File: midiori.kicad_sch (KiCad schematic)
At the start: 86 parts, among them J1 midiori-rescue_x68000_expansi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, J2 Conn_ARM_JTAG_SWD_10, J3 AudioJack3, J4 Mini-DIN-5, J5 AudioJack3, J6 AudioJack3, J7 Conn_01x06, J8 AudioJack3, J9 Mini-DIN-5, U1 74LCX07, U10 ICE40HX1K-VQ100, U11 AP2205K-3.3, U12 AK4432, U13 TL074, U14 AP2205K-3.3, U15 TL072, U16 74LCX07, U17 PC817, U18 SN74LVC245APW, U2 AT25SF081-SSHD-X, U3 AP2127K-1.2, U4 SN74LVC245APW, U5 SN74LVC245APW, U6 SN74LVC245APW, U7 SN74LVC245APW, U8 SN74LVC245APW, U9 SN74LVC245APW, X1 16MHz, X2 24.576MHz

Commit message: aaaaaaaaaaa
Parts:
- removed C11, C13, C15, C4, C6, C9: 0.1uF, Capacitor_SMD:C_0805_2012Metric, symbol Device:C
- added JP3, JP4, JP5: Jumper_3_Bridged12, Jumper:SolderJumper-3_P1.3mm_Bridged12_Pad1.0x1.5mm, symbol Jumper:Jumper_3_Bridged12
- added unit 6 of U1
- R14: value R -> 10k; footprint (none) -> Resistor_SMD:R_0805_2012Metric
- R15, R16: footprint (none) -> Resistor_SMD:R_0805_2012Metric
- R6, R9: footprint Resistor_SMD:R_0805_2012Metric_Pad1.15x1.40mm_HandSolder -> Resistor_SMD:R_0805_2012Metric
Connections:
- net +3V3: now also U18.1 (DIR), U8.1 (DIR)
- net 10m: now also U10.89 (IOT_84_GBIN1); no longer U10.97 (IOT_91)
- net 24.576mhz: now also JP5.1 (A)
- net BG: now also J1.B47 (/BG), U18.2 (A1); no longer U18.18 (B1)
- net BGACK: now also J1.B48 (/BGACK)
- net BR: now also J1.B46 (/BR)
- net DTACK: now also U18.5 (A4)
- net EXOWN: now also J1.B39 (/EXOWN), U18.4 (A3)
- net EXREQ: now also J1.B36 (/EXREQ)
- net GND: now also U18.11 (B8), U18.12 (B7), U18.13 (B6), U18.7 (A6), U18.8 (A7), U18.9 (A8); no longer U18.1 (DIR), U8.1 (DIR)
- net IDDIR: now also U8.9 (A8), JP3.1 (A)
- net RW: now also U16.8
- net UDS: now also U18.3 (A2), U1.12; no longer U16.8, U18.17 (B2)
- net addr_dir: now also JP4.3 (B); no longer U10.69 (IOR_68)
- net bg: now also U18.18 (B1); no longer U18.2 (A1)
- net bick: now also JP5.2 (C); no longer U10.89 (IOT_84_GBIN1)
- net data_dir: now also U10.69 (IOR_68), JP3.2 (C), JP3.3 (B); no longer U10.96 (IOT_90)
- net dtack: now also U10.82 (IOT_78), U18.15 (B4); no longer U1.5, U10.93 (IOT_87)
- net exown: now also U10.97 (IOT_91), U18.16 (B3); no longer U10.82 (IOT_78), U16.1
- net rw_drv: now also U16.9
- net uds: now also U18.17 (B2), JP4.1 (A); no longer U10.83 (IOT_79), U18.3 (A2)
- net uds_lds_drv: now also U1.13; no longer U16.9
- net EXACK: now reaches J1.B37 (/EXACK)
- net EXACK: now also U18.6 (A5)
- net iddir: now reaches U8.11 (B8)
- net iddir: now also U10.96 (IOT_90)
- net exack: now reaches U18.14 (B5)
- net exreq renamed exreq_drv
- new net: JP4.2 (C), JP5.3 (B), U10.83 (IOT_79)
- new net dtack_drv: U1.5, U10.93 (IOT_87)
- new net exown_drv: U16.1
- no-connect marks 48 -> 33
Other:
- moved on the sheet: U16D

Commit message: swap optos
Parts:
- removed JP3, JP4, JP5: Jumper_3_Bridged12, Jumper:SolderJumper-3_P1.3mm_Bridged12_Pad1.0x1.5mm, symbol Jumper:Jumper_3_Bridged12
- removed U10: ICE40HX1K-VQ100, ICE40HX1K-VQ100:QFP50P1600X1600X120-100N, symbol midiori-rescue:ICE40HX1K-VQ100-ICE40HX1K-VQ100-midiori-rescue-midiori-rescue
- added C11, C13, C4, C6, C9: 0.1uF, Capacitor_SMD:C_0805_2012Metric, symbol Device:C
- added U10: ICE40HX1K-TQ144, Package_QFP:TQFP-144_20x20mm_P0.5mm, symbol FPGA_Lattice:ICE40HX1K-TQ144
- J1: footprint x68k:x68000_expansion -> x68k:x68000_expansion_vias
- U17: value PC817 -> H11L1; footprint Package_DIP:DIP-4_W7.62mm -> Package_DIP:SMDIP-6_W9.53mm; symbol Isolator:PC817 -> Isolator:H11L1
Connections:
- net +1V2: now also U10.111 (VCC), U10.27 (VCC), U10.36 (VCCPLL), U10.51 (VCC), U10.92 (VCC)
- net +3V3: now also U17.6, C11.1, C13.1, C4.1, C6.1, C9.1, U10.100 (VCCIO_1), U10.108 (VPP_2V5), U10.123 (VCCIO_0), U10.133 (VCCIO_0), U10.30 (VCCIO_3), U10.46 (VCCIO_2), U10.57 (VCCIO_2), U10.6 (VCCIO_3), U10.72 (VCC_SPI), U10.89 (VCCIO_1)
- net 10MHz: now also U8.9 (A8); no longer U8.2 (A1)
- net 10m: now also U8.11 (B8), U10.144 (IOT_96); no longer U8.18 (B1)
- net 16mhz: now also U10.93 (IOR_60_GBIN3)
- net 24.576mhz: now also U10.94 (IOR_61_GBIN2)
- net AS: now also U16.8, U8.8 (A7); no longer U16.6, U8.6 (A5)
- net BG: now also U18.5 (A4); no longer U18.2 (A1)
- net BGACK: now also U1.2; no longer U16.10
- net BR: now also U1.4; no longer U1.10
- net DTACK: now also U16.12, U8.3 (A2); no longer U1.6, U18.5 (A4)
- net EXACK: now also U8.2 (A1); no longer U18.6 (A5)
- net EXOWN: now also U1.6, U18.8 (A7); no longer U16.2, U18.4 (A3)
- net EXREQ: now also U16.2; no longer U16.4
- net EXRESET: now also U18.9 (A8); no longer U8.3 (A2)
- net GND: now also U17.5, C11.2, C13.2, C4.2, C6.2, C9.2, U10.103 (GND), U10.13 (GND), U10.132 (GND), U10.14 (GND), U10.140 (GND), U10.35 (GNDPLL), U10.5 (GND), U10.59 (GND), U10.69 (GND), U10.86 (GND); no longer U17.3, U18.11 (B8), U18.12 (B7), U18.13 (B6), U18.7 (A6), U18.8 (A7), U18.9 (A8)
- net IACK2: now also U18.7 (A6); no longer U8.7 (A6)
- net IACK4: now also U18.6 (A5); no longer U8.8 (A7)
- net IDDIR: now also U8.4 (A3); no longer U8.9 (A8)
- net IRQ2: now also U1.8; no longer U1.2
- net IRQ4: now also U1.10; no longer U1.4
- net LDS: now also U16.6, U8.7 (A6); no longer U16.12, U8.5 (A4)
- net RW: now also U16.4, U8.5 (A4); no longer U16.8, U8.4 (A3)
- net UDS: now also J1.A29 (/UDS), U16.10, U8.6 (A5); no longer U1.12, U18.3 (A2)
- net a1: now also U10.58 (IOB_38)
- net a16: now also U10.11 (IOL_5A)
- net a17: now also U10.10 (IOL_4B)
- net a18: now also U10.9 (IOL_4A)
- net a19: now also U10.8 (IOL_3B)
- net a2: now also U10.56 (IOB_37)
- net a20: now also U10.7 (IOL_3A)
- net a21: now also U10.4 (IOL_2B)
- net a22: now also U10.3 (IOL_2A)
- net a23: now also U10.2 (IOL_1B)
- net a3: now also U10.52 (IOB_34)
- net a4: now also U10.50 (IOB_36_GBIN4)
- net a5: now also U10.49 (IOB_35_GBIN5)
- net a6: now also U10.48 (IOB_33)
- net a7: now also U10.47 (IOB_32)
- net ab10: now also U10.33 (IOL_12A)
- net ab11: now also U10.32 (IOL_11B)
- net ab12: now also U10.31 (IOL_11A)
- net ab13: now also U10.29 (IOL_10B)
- net ab14: now also U10.28 (IOL_10A)
- net ab15: now also U10.26 (IOL_9B)
- net ab9: now also U10.34 (IOL_12B)
- net addr_dir: now also U10.61 (IOB_40)
- net as: now also U8.12 (B7), U10.143 (IOT_95); no longer U8.14 (B5)
- net as_drv: now also U16.9, U10.121 (IOT_82); no longer U16.5
- net bg: now also U18.15 (B4), U10.122 (IOT_83); no longer U18.18 (B1)
- net bgack: now also U1.1, U10.107 (IOR_72); no longer U16.11
- net bick: now also U10.76 (IOR_51)
- net br: now also U1.3, U10.113 (IOT_74); no longer U1.11
- net d0: now also U10.45 (IOB_31)
- net d1: now also U10.44 (IOB_30)
- net d2: now also U10.43 (IOB_29)
- net d3: now also U10.42 (IOB_28)
- net d4: now also U10.41 (IOB_27)
- net d5: now also U10.39 (IOB_26)
- net d6: now also U10.38 (IOB_25)
- net d7: now also U10.37 (IOB_24)
- net data_dir: now also U10.60 (IOB_39)
- net db10: now also U10.23 (IOL_8A)
- net db11: now also U10.22 (IOL_7B)
- net db12: now also U10.21 (IOL_7A_GBIN6)
- net db13: now also U10.20 (IOL_6B_GBIN7)
- net db14: now also U10.19 (IOL_6A)
- net db15: now also U10.12 (IOL_5B)
- net db8: now also U10.25 (IOL_9A)
- net db9: now also U10.24 (IOL_8B)
- net dtack: now also U8.17 (B2), U10.137 (IOT_90); no longer U18.15 (B4)
- net dtack_drv: now also U16.13, U10.117 (IOT_78); no longer U1.5
- net exack: now also U8.18 (B1), U10.136 (IOT_89); no longer U18.14 (B5)
- net exown: now also U18.12 (B7), U10.134 (IOT_87); no longer U18.16 (B3)
- net exown_drv: now also U1.5, U10.114 (IOT_75); no longer U16.1
- net exreq_drv: now also U16.1, U10.116 (IOT_77); no longer U16.3
- net exreset: now also U18.11 (B8), U10.135 (IOT_88); no longer U8.17 (B2)
- net iack2: now also U18.13 (B6), U10.129 (IOT_85_GBIN0); no longer U8.13 (B6)
- net iack4: now also U18.14 (B5), U10.128 (IOT_84_GBIN1); no longer U8.12 (B7)
- net iddir: now also U8.16 (B3), U10.138 (IOT_91); no longer U8.11 (B8)
- net irq2: now also U1.9, U10.115 (IOT_76); no longer U1.1
- net irq4: now also U1.11, U10.112 (IOT_73); no longer U1.3
- net lds: now also U8.13 (B6), U10.142 (IOT_94); no longer U8.15 (B4)
- net lrck: now also U10.74 (IOR_49)
- net midi_in: now also U10.104 (IOR_69)
- net midi_out: now also U1.13, U10.105 (IOR_70); no longer U1.9
- net reset: now also U10.66 (~{CRESET_B})
- net rw: now also U8.15 (B4), U10.139 (IOT_92); no longer U8.16 (B3)
- net rw_drv: now also U16.3, U10.118 (IOT_79); no longer U16.9
- net sck: now also U10.70 (IOB_46_SCK)
- net sdti: now also U10.75 (IOR_50)
- net si: now also U10.67 (IOB_44_SDO)
- net smute: now also U10.73 (IOR_48)
- net so: now also U10.68 (IOB_45_SDI)
- net ss: now also U10.71 (IOB_47_SS)
- net uds: now also U8.14 (B5), U10.141 (IOT_93); no longer U18.17 (B2)
- net xltr_oe: now also U10.62 (IOB_41)
- net at R9.2: now also U1.12; no longer U1.8
- removed net uds_lds_drv: U1.13, U16.13
- new net lds_drv: U10.120 (IOT_81), U16.5
- new net uds_drv: U10.119 (IOT_80), U16.11
- no-connect marks 33 -> 32
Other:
- moved on the sheet: C10, C12, C14, C3, C5, C7, R3, U16A, U16B, U16C, U16D, U16E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

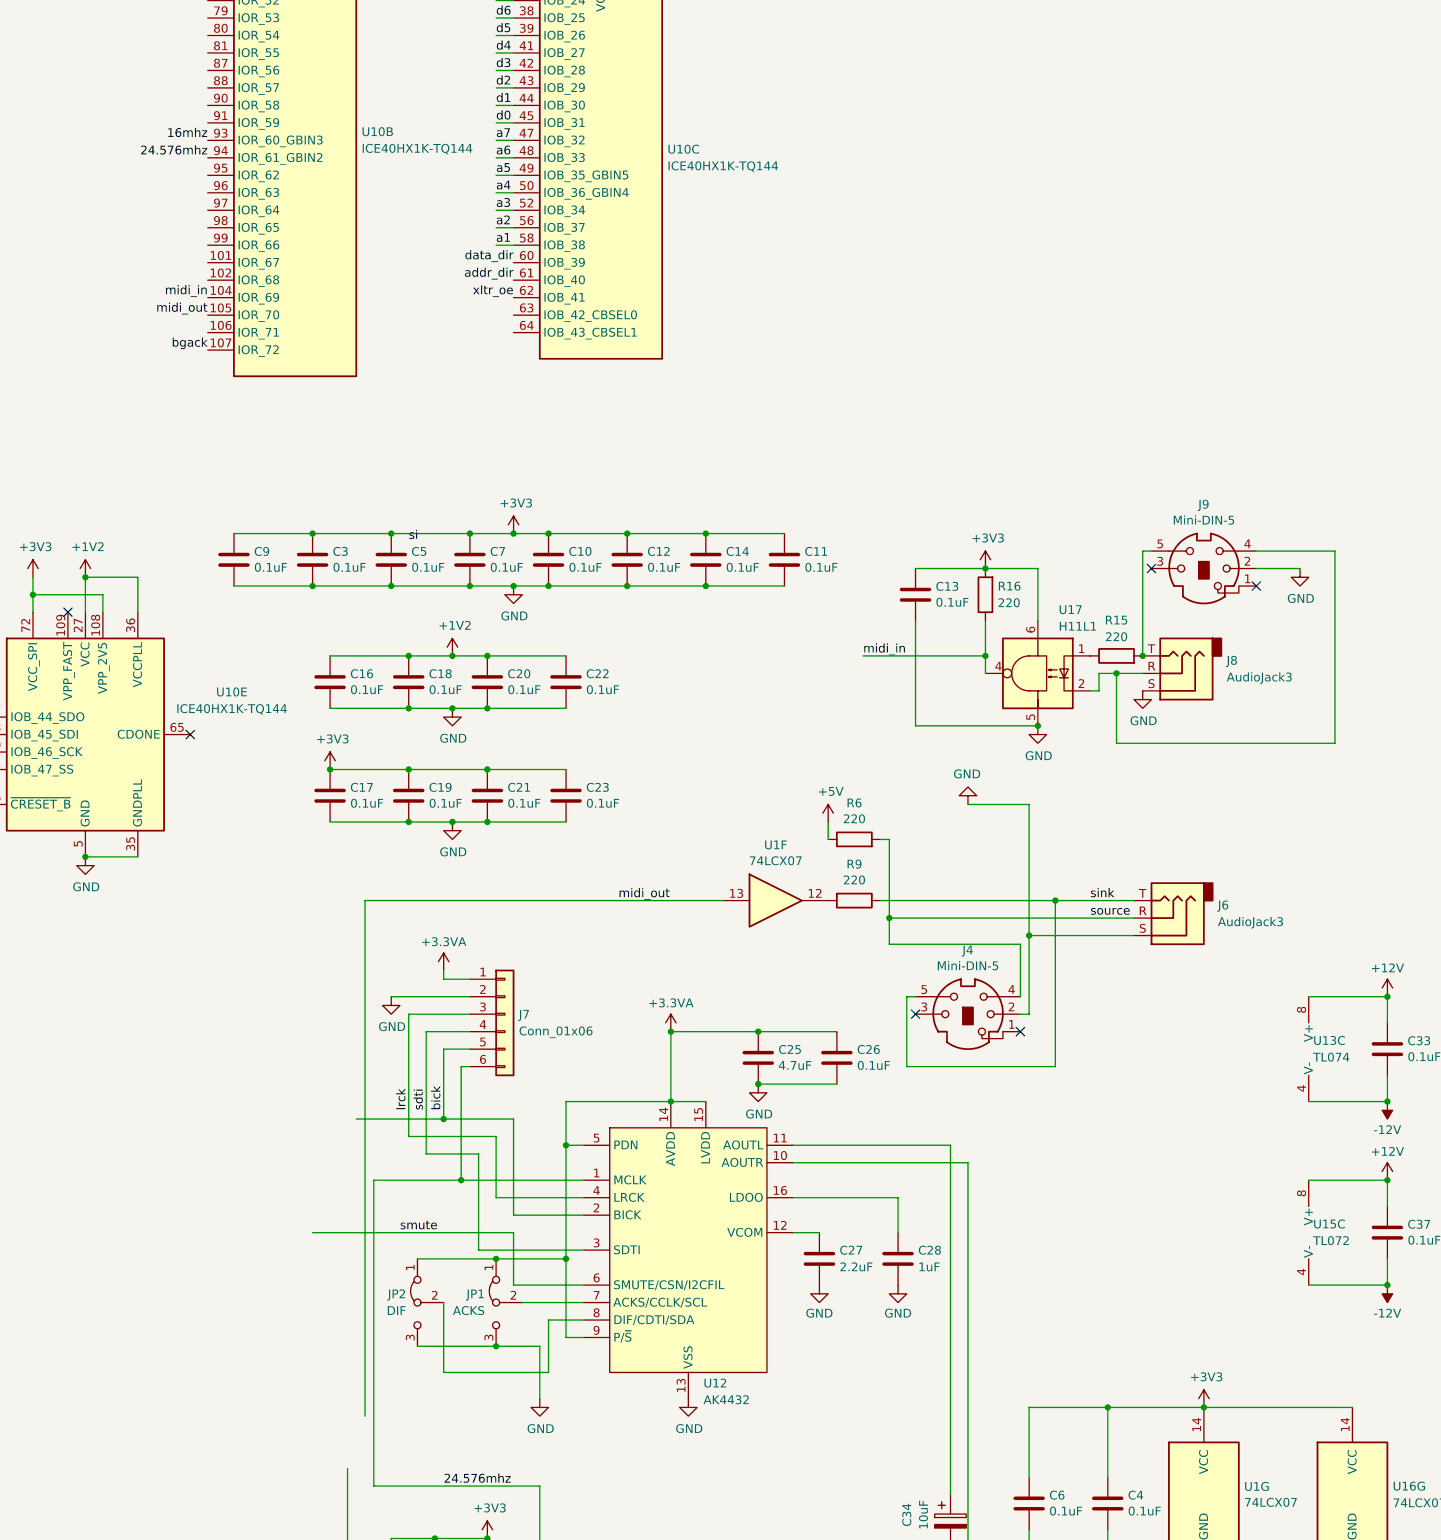
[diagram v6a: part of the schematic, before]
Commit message: crystal swap
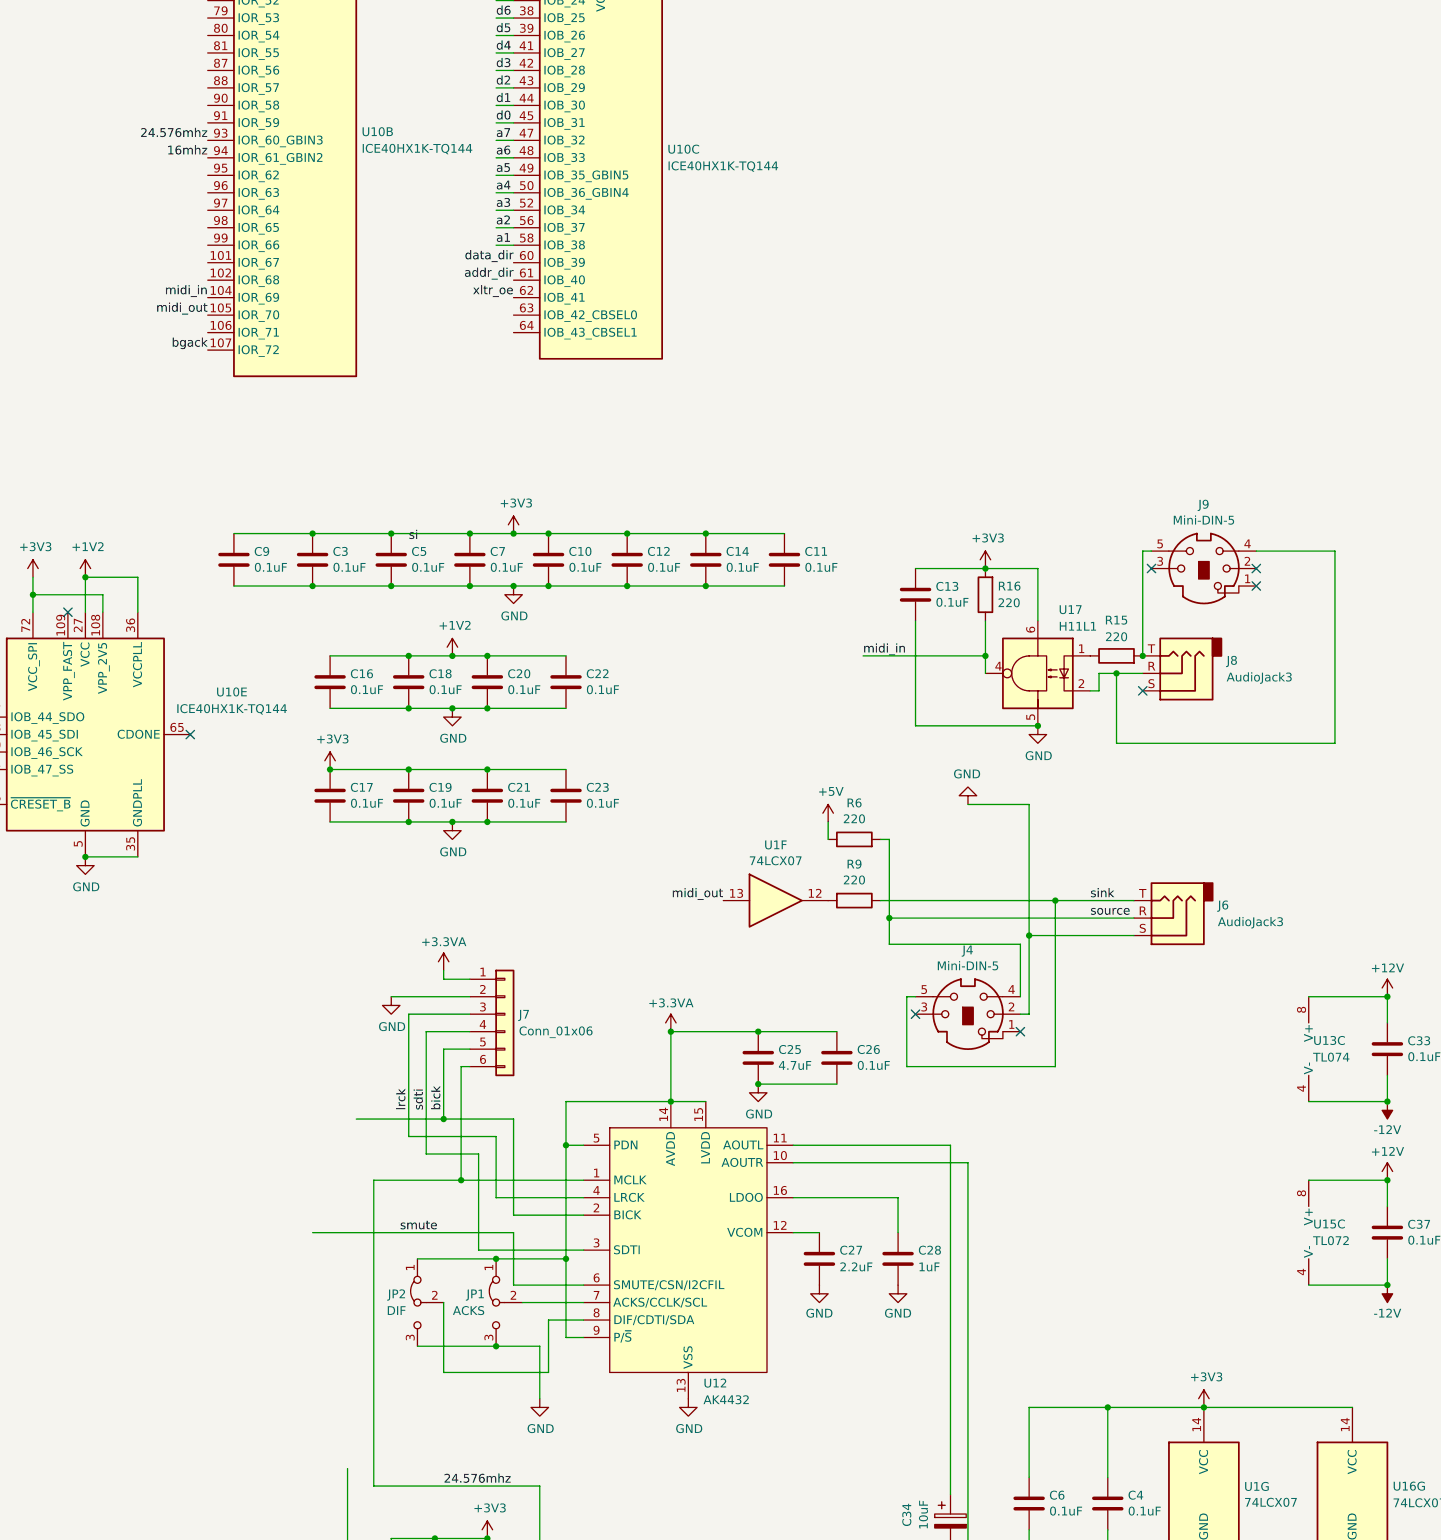
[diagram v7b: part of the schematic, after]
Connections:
- net 16mhz: now also U10.94 (IOR_61_GBIN2); no longer U10.93 (IOR_60_GBIN3)
- net 24.576mhz: now also U10.93 (IOR_60_GBIN3); no longer U10.94 (IOR_61_GBIN2)
- net GND: no longer J8.S, J9.2
- no-connect marks 32 -> 34
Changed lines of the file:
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@@
 	)
 	(no_connect
+		(at 377.19 41.91)
+	)
+	(no_connect
 		(at 58.42 166.37)
 	)
@@
 	)
 	(no_connect
+		(at 393.7 24.13)
+	)
+	(no_connect
 		(at 58.42 179.07)
 	)
@@
 	(wire
 		(pts
-			(xy 264.16 72.39) (xy 316.23 72.39)
-		)
-		(stroke
-			(width 0)
-			(type default)
-		)
-	)
-	(wire
-		(pts
 			(xy 283.21 -58.42) (xy 285.75 -58.42)
 		)
@@
 	(wire
 		(pts
-			(xy 264.16 147.32) (xy 264.16 72.39)
-		)
-		(stroke
-			(width 0)
-			(type default)
-		)
-	)
-	(wire
-		(pts
 			(xy 175.26 45.72) (xy 158.75 45.72)
 		)
@@
 	(wire
 		(pts
-			(xy 393.7 24.13) (xy 400.05 24.13)
-		)
-		(stroke
-			(width 0)
-			(type default)
-		)
-	)
-	(wire
-		(pts
 			(xy 384.81 220.98) (xy 381 220.98)
 		)
@@
 	)
 	(label "24.576mhz"
-		(at 241.3 -35.56 180)
+		(at 241.3 -38.1 180)
 		(fields_autoplaced yes)
 		(effects
@@
 	)
 	(label "midi_out"
-		(at 300.99 72.39 0)
+		(at 316.23 72.39 180)
 		(fields_autoplaced yes)
 		(effects
@@
 				(size 1.27 1.27)
 			)
-			(justify left bottom)
+			(justify right bottom)
 		)
 	)
@@
 	)
 	(label "16mhz"
-		(at 241.3 -38.1 180)
+		(at 241.3 -35.56 180)
 		(fields_autoplaced yes)
 		(effects
@@
 	)
 	(symbol
-		(lib_id "midiori-rescue:GND-power")
-		(at 377.19 41.91 0)
-		(unit 1)
-		(exclude_from_sim no)
-		(in_bom yes)
-		(on_board yes)
-		(dnp no)
-		(property "Reference" "#PWR041"
-			(at 377.19 48.26 0)
-			(effects
-				(font
-					(size 1.27 1.27)
-				)
-				(hide yes)
-			)
-		)
-		(property "Value" "GND"
-			(at 377.317 46.3042 0)
-			(effects
-				(font
-					(size 1.27 1.27)
-				)
-			)
-		)
-		(property "Footprint" ""
-			(at 377.19 41.91 0)
-			(effects
-				(font
-					(size 1.27 1.27)
-				)
-				(hide yes)
-			)
-		)
-		(property "Datasheet" ""
-			(at 377.19 41.91 0)
-			(effects
-				(font
-					(size 1.27 1.27)
-				)
-				(hide yes)
-			)
-		)
-		(property "Description" ""
-			(at 377.19 41.91 0)
-			(effects
-				(font
-					(size 1.27 1.27)
-				)
-				(hide yes)
-			)
-		)
-		(pin "1"
-		)
-		(instances
-			(project "midiori"
-				(path "/89a089da-4491-480f-b113-8450a227c3da"
-					(reference "#PWR041")
-					(unit 1)
-				)
-			)
-		)
-	)
-	(symbol
 		(lib_id "Device:R")
 		(at 373.38 36.83 90)
@@
 				)
 			)
-		)
-	)
-	(symbol
-		(lib_id "midiori-rescue:GND-power")
-		(at 400.05 24.13 0)
-		(unit 1)
-		(exclude_from_sim no)
-		(in_bom yes)
-		(on_board yes)
-		(dnp no)
-		(property "Reference" "#PWR044"
-			(at 400.05 30.48 0)
-			(effects
-				(font
-					(size 1.27 1.27)
-				)
-				(hide yes)
-			)
-		)
-		(property "Value" "GND"
-			(at 400.177 28.5242 0)
-			(effects
-				(font
-					(size 1.27 1.27)
-				)
-			)
-		)
-		(property "Footprint" ""
-			(at 400.05 24.13 0)
-			(effects
-				(font
-					(size 1.27 1.27)
-				)
-				(hide yes)
-			)
-		)
-		(property "Datasheet" ""
-			(at 400.05 24.13 0)
-			(effects
-				(font
-					(size 1.27 1.27)
-				)
-				(hide yes)
-			)
-		)
-		(property "Description" ""
-			(at 400.05 24.13 0)
-			(effects
-				(font
-					(size 1.27 1.27)
-				)
-				(hide yes)
-			)
-		)
-		(pin "1"
-		)
-		(instances
-			(project "midiori"
-				(path "/89a089da-4491-480f-b113-8450a227c3da"
-					(reference "#PWR044")
-					(unit 1)
-				)
-			)

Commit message: missing wire
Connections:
- net GND: now also U18.16 (B3), U18.17 (B2), U18.18 (B1), U18.2 (A1), U18.3 (A2), U18.4 (A3)
- net a16: now also U10.10 (IOL_4B); no longer U10.11 (IOL_5A)
- net a17: now also U10.9 (IOL_4A); no longer U10.10 (IOL_4B)
- net a18: now also U10.8 (IOL_3B); no longer U10.9 (IOL_4A)
- net a19: now also U10.7 (IOL_3A); no longer U10.8 (IOL_3B)
- net a20: now also U10.4 (IOL_2B); no longer U10.7 (IOL_3A)
- net a21: now also U10.3 (IOL_2A); no longer U10.4 (IOL_2B)
- net a22: now also U10.2 (IOL_1B); no longer U10.3 (IOL_2A)
- net a23: now also U10.1 (IOL_1A); no longer U10.2 (IOL_1B)
- net ab10: now also U10.32 (IOL_11B); no longer U10.33 (IOL_12A)
- net ab11: now also U10.31 (IOL_11A); no longer U10.32 (IOL_11B)
- net ab12: now also U10.29 (IOL_10B); no longer U10.31 (IOL_11A)
- net ab13: now also U10.28 (IOL_10A); no longer U10.29 (IOL_10B)
- net ab14: now also U10.26 (IOL_9B); no longer U10.28 (IOL_10A)
- net ab15: now also U10.25 (IOL_9A); no longer U10.26 (IOL_9B)
- net ab8: now also U10.34 (IOL_12B)
- net ab9: now also U10.33 (IOL_12A); no longer U10.34 (IOL_12B)
- net db10: now also U10.22 (IOL_7B); no longer U10.23 (IOL_8A)
- net db11: now also U10.21 (IOL_7A_GBIN6); no longer U10.22 (IOL_7B)
- net db12: now also U10.20 (IOL_6B_GBIN7); no longer U10.21 (IOL_7A_GBIN6)
- net db13: now also U10.19 (IOL_6A); no longer U10.20 (IOL_6B_GBIN7)
- net db14: now also U10.12 (IOL_5B); no longer U10.19 (IOL_6A)
- net db15: now also U10.11 (IOL_5A); no longer U10.12 (IOL_5B)
- net db8: now also U10.24 (IOL_8B); no longer U10.25 (IOL_9A)
- net db9: now also U10.23 (IOL_8A); no longer U10.24 (IOL_8B)
- no-connect marks 34 -> 52
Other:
- moved on the sheet: U10B, U10C
